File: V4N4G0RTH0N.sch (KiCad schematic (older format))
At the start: 125 parts, among them SW1 SW_Push, U1 ATmega32U4-A, Y1 16MHz

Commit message: I think I'm done??
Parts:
- removed F1, F2: Polyfuse_Small, Fuse:Fuse_1206_3216Metric, symbol V4N4G0RTH0N-rescue:Polyfuse_Small-Device
- removed R3: 10k, Resistor_SMD:R_0805_2012Metric, symbol V4N4G0RTH0N-rescue:R_Small-Device
- removed SW1: SW_Push, random-keyboard-parts:SKQG-1155865, symbol V4N4G0RTH0N-rescue:SW_Push-Switch
- added U2: SRV05-4, Package_TO_SOT_SMD:SOT-23-6, symbol Power_Protection:SRV05-4
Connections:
- wire segments 231 -> 226
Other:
- moved on the sheet: R8, R9

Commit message: V2
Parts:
- added D54: SOD-123, Diode_SMD:D_SOD-123, symbol V4N4G0RTH0N-rescue:D_Small-Device
- added F1: 500mA, symbol Device:Polyfuse_Small
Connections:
- net +5V: now also F1.1
- net GND: now also D54.1 (K)
- net VCC: now also F1.2
- net at U1.13 (~RESET): now also D54.2 (A)
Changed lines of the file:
@@
 Wire Wire Line
 	4600 7450 5000 7450
+$Comp
+L V4N4G0RTH0N-rescue:D_Small-Device D54
+U 1 1 5FDBF20F
+P 1700 2000
+F 0 "D54" H 1600 2150 50  0000 R CNN
+F 1 "SOD-123" H 2000 2150 50  0000 R CNN
+F 2 "Diode_SMD:D_SOD-123" V 1700 2000 50  0001 C CNN
+F 3 "~" V 1700 2000 50  0001 C CNN
+	1    1700 2000
+	1    0    0    -1
+$EndComp
+$Comp
+L V4N4G0RTH0N-rescue:GND-power #PWR01
+U 1 1 5FDE02C4
+P 1350 2000
+F 0 "#PWR01" H 1350 1750 50  0001 C CNN
+F 1 "GND" H 1355 1827 50  0000 C CNN
+F 2 "" H 1350 2000 50  0001 C CNN
+F 3 "" H 1350 2000 50  0001 C CNN
+	1    1350 2000
+	1    0    0    -1
+$EndComp
+Wire Wire Line
+	1350 2000 1600 2000
+Wire Wire Line
+	1800 2000 2000 2000
+$Comp
+L power:VCC #PWR?
+U 1 1 5FF8CE96
+P 1550 9050
+F 0 "#PWR?" H 1550 8900 50  0001 C CNN
+F 1 "VCC" H 1565 9223 50  0000 C CNN
+F 2 "" H 1550 9050 50  0001 C CNN
+F 3 "" H 1550 9050 50  0001 C CNN
+	1    1550 9050
+	1    0    0    -1
+$EndComp
+$Comp
+L power:+5V #PWR?
+U 1 1 5FF8DDFE
+P 2350 9050
+F 0 "#PWR?" H 2350 8900 50  0001 C CNN
+F 1 "+5V" H 2365 9223 50  0000 C CNN
+F 2 "" H 2350 9050 50  0001 C CNN
+F 3 "" H 2350 9050 50  0001 C CNN
+	1    2350 9050
+	1    0    0    -1
+$EndComp
+$Comp
+L Device:Polyfuse_Small F1
+U 1 1 5FF90039
+P 1950 9050
+F 0 "F1" V 1745 9050 50  0000 C CNN
+F 1 "500mA" V 1836 9050 50  0000 C CNN
+F 2 "" H 2000 8850 50  0001 L CNN
+F 3 "~" H 1950 9050 50  0001 C CNN
+	1    1950 9050
+	0    1    1    0
+$EndComp
+Wire Wire Line
+	1550 9050 1850 9050
+Wire Wire Line
+	2050 9050 2350 9050
 $EndSCHEMATC

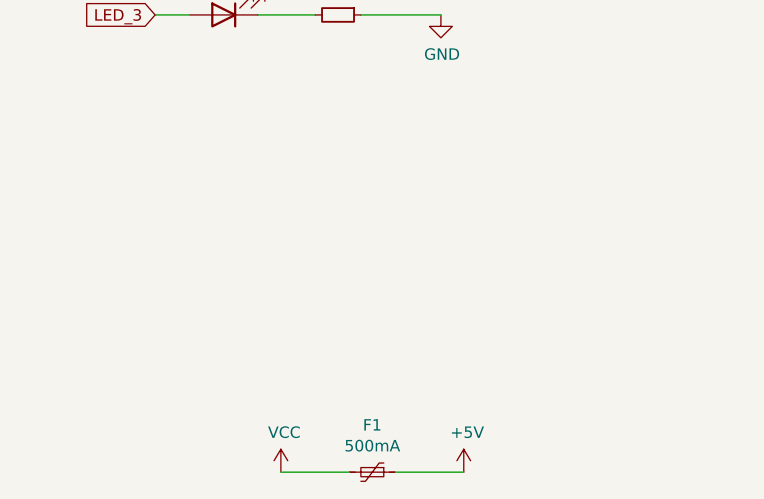
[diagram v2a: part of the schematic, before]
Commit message: V2 sch changes
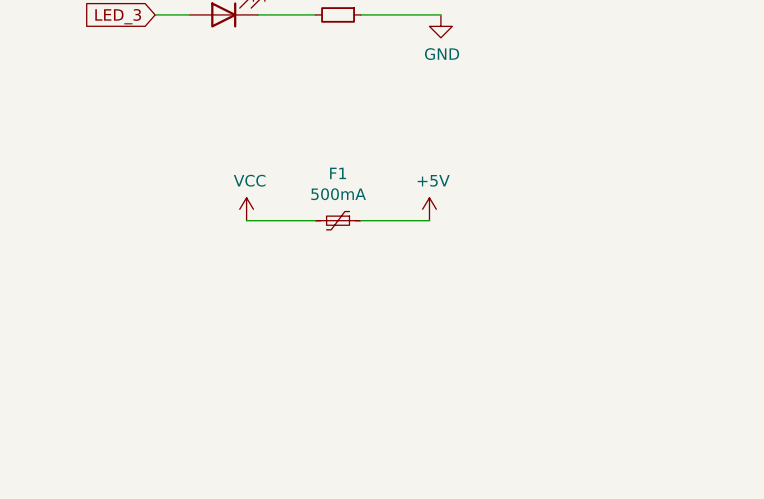
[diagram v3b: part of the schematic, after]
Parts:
- F1: footprint (none) -> Fuse:Fuse_0805_2012Metric
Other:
- moved on the sheet: F1
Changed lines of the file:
@@
 	1800 2000 2000 2000
 $Comp
-L power:VCC #PWR?
+L power:VCC #PWR0109
 U 1 1 5FF8CE96
-P 1550 9050
-F 0 "#PWR?" H 1550 8900 50  0001 C CNN
-F 1 "VCC" H 1565 9223 50  0000 C CNN
-F 2 "" H 1550 9050 50  0001 C CNN
-F 3 "" H 1550 9050 50  0001 C CNN
-	1    1550 9050
+P 1400 7950
+F 0 "#PWR0109" H 1400 7800 50  0001 C CNN
+F 1 "VCC" H 1415 8123 50  0000 C CNN
+F 2 "" H 1400 7950 50  0001 C CNN
+F 3 "" H 1400 7950 50  0001 C CNN
+	1    1400 7950
 	1    0    0    -1
 $EndComp
 $Comp
-L power:+5V #PWR?
+L power:+5V #PWR0110
 U 1 1 5FF8DDFE
-P 2350 9050
-F 0 "#PWR?" H 2350 8900 50  0001 C CNN
-F 1 "+5V" H 2365 9223 50  0000 C CNN
-F 2 "" H 2350 9050 50  0001 C CNN
-F 3 "" H 2350 9050 50  0001 C CNN
-	1    2350 9050
+P 2200 7950
+F 0 "#PWR0110" H 2200 7800 50  0001 C CNN
+F 1 "+5V" H 2215 8123 50  0000 C CNN
+F 2 "" H 2200 7950 50  0001 C CNN
+F 3 "" H 2200 7950 50  0001 C CNN
+	1    2200 7950
 	1    0    0    -1
 $EndComp
@@
 L Device:Polyfuse_Small F1
 U 1 1 5FF90039
-P 1950 9050
-F 0 "F1" V 1745 9050 50  0000 C CNN
-F 1 "500mA" V 1836 9050 50  0000 C CNN
-F 2 "" H 2000 8850 50  0001 L CNN
-F 3 "~" H 1950 9050 50  0001 C CNN
-	1    1950 9050
+P 1800 7950
+F 0 "F1" V 1595 7950 50  0000 C CNN
+F 1 "500mA" V 1686 7950 50  0000 C CNN
+F 2 "Fuse:Fuse_0805_2012Metric" H 1850 7750 50  0001 L CNN
+F 3 "~" H 1800 7950 50  0001 C CNN
+	1    1800 7950
 	0    1    1    0
 $EndComp
 Wire Wire Line
-	1550 9050 1850 9050
+	1400 7950 1700 7950
 Wire Wire Line
-	2050 9050 2350 9050
+	1900 7950 2200 7950
 $EndSCHEMATC

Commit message: V4N v2
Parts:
- added C8: 4.7n, Capacitor_SMD:C_0805_2012Metric, symbol Device:C_Small
- added R10: 1M, Resistor_SMD:R_0805_2012Metric, symbol Device:R_Small
- added R3: 10k, Resistor_SMD:R_0805_2012Metric, symbol Device:R_Small
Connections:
- net +5V: now also R3.1
- net GND: now also C8.1, R10.1; no longer USB1.13 (SHIELD)
- net at D54.2 (A), U1.13 (~RESET): now also R3.2
- new net Earth: C8.2, R10.2, USB1.13 (SHIELD)
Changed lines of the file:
@@
 $EndComp
-Wire Wire Line
-	4500 7450 4600 7450
 Wire Wire Line
 	4500 6750 5650 6750
@@
 Wire Wire Line
 	5700 6300 6200 6300
-Wire Wire Line
-	4500 7550 4600 7550
-Wire Wire Line
-	4600 7550 4600 7450
-Connection ~ 4600 7450
-Wire Wire Line
-	4600 7450 5000 7450
 $Comp
 L V4N4G0RTH0N-rescue:D_Small-Device D54
 U 1 1 5FDBF20F
 P 1700 2000
-F 0 "D54" H 1600 2150 50  0000 R CNN
-F 1 "SOD-123" H 2000 2150 50  0000 R CNN
+F 0 "D54" H 1750 2100 50  0000 R CNN
+F 1 "SOD-123" H 1850 1900 50  0000 R CNN
 F 2 "Diode_SMD:D_SOD-123" V 1700 2000 50  0001 C CNN
 F 3 "~" V 1700 2000 50  0001 C CNN
@@
 	1350 2000 1600 2000
 Wire Wire Line
-	1800 2000 2000 2000
+	1800 2000 1850 2000
 $Comp
 L power:VCC #PWR0109
@@
 Wire Wire Line
 	1900 7950 2200 7950
+$Comp
+L Device:R_Small R3
+U 1 1 5FFE33EE
+P 1850 1700
+F 0 "R3" H 1909 1746 50  0000 L CNN
+F 1 "10k" H 1909 1655 50  0000 L CNN
+F 2 "Resistor_SMD:R_0805_2012Metric" H 1850 1700 50  0001 C CNN
+F 3 "~" H 1850 1700 50  0001 C CNN
+	1    1850 1700
+	1    0    0    -1
+$EndComp
+$Comp
+L power:+5V #PWR0122
+U 1 1 5FFE46B1
+P 1850 1450
+F 0 "#PWR0122" H 1850 1300 50  0001 C CNN
+F 1 "+5V" H 1865 1623 50  0000 C CNN
+F 2 "" H 1850 1450 50  0001 C CNN
+F 3 "" H 1850 1450 50  0001 C CNN
+	1    1850 1450
+	1    0    0    -1
+$EndComp
+Wire Wire Line
+	1850 2000 1850 1800
+Connection ~ 1850 2000
+Wire Wire Line
+	1850 2000 2000 2000
+Wire Wire Line
+	1850 1600 1850 1450
+Wire Wire Line
+	4500 7450 5000 7450
+$Comp
+L power:Earth #PWR0123
+U 1 1 6004768E
+P 4500 7600
+F 0 "#PWR0123" H 4500 7350 50  0001 C CNN
+F 1 "Earth" H 4500 7450 50  0001 C CNN
+F 2 "" H 4500 7600 50  0001 C CNN
+F 3 "~" H 4500 7600 50  0001 C CNN
+	1    4500 7600
+	1    0    0    -1
+$EndComp
+Wire Wire Line
+	4500 7550 4500 7600
+$Comp
+L power:Earth #PWR0124
+U 1 1 60059175
+P 3900 7900
+F 0 "#PWR0124" H 3900 7650 50  0001 C CNN
+F 1 "Earth" H 3900 7750 50  0001 C CNN
+F 2 "" H 3900 7900 50  0001 C CNN
+F 3 "~" H 3900 7900 50  0001 C CNN
+	1    3900 7900
+	0    1    1    0
+$EndComp
+$Comp
+L Device:R_Small R10
+U 1 1 60079CBD
+P 4150 7900
+F 0 "R10" V 3954 7900 50  0000 C CNN
+F 1 "1M" V 4045 7900 50  0000 C CNN
+F 2 "Resistor_SMD:R_0805_2012Metric" H 4150 7900 50  0001 C CNN
+F 3 "~" H 4150 7900 50  0001 C CNN
+	1    4150 7900
+	0    1    1    0
+$EndComp
+$Comp
+L Device:C_Small C8
+U 1 1 6007AEF1
+P 4150 8250
+F 0 "C8" V 3921 8250 50  0000 C CNN
+F 1 "4.7n" V 4012 8250 50  0000 C CNN
+F 2 "Capacitor_SMD:C_0805_2012Metric" H 4150 8250 50  0001 C CNN
+F 3 "~" H 4150 8250 50  0001 C CNN
+	1    4150 8250
+	0    1    1    0
+$EndComp
+$Comp
+L power:GND #PWR0125
+U 1 1 6007C3AC
+P 4400 7900
+F 0 "#PWR0125" H 4400 7650 50  0001 C CNN
+F 1 "GND" V 4405 7772 50  0000 R CNN
+F 2 "" H 4400 7900 50  0001 C CNN
+F 3 "" H 4400 7900 50  0001 C CNN
+	1    4400 7900
+	0    -1   -1   0
+$EndComp
+Wire Wire Line
+	3900 7900 4050 7900
+Wire Wire Line
+	4050 7900 4050 8250
+Connection ~ 4050 7900
+Wire Wire Line
+	4250 8250 4250 7900
+Wire Wire Line
+	4250 7900 4400 7900
+Connection ~ 4250 7900
 $EndSCHEMATC

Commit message: Add slider
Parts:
- added RV1: R_Potentiometer, Potentiometer_THT:Potentiometer_Bourns_PTA3043_Single_Slide, symbol Device:R_Potentiometer
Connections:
- net +5V: now also RV1.3
- net COL11: now also U1.8 (PB0); no longer U1.41 (PF0)
- net GND: now also RV1.1
- new net ANAL_IN: RV1.2, U1.41 (PF0)
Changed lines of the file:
@@
 Text GLabel 3200 4500 2    50   Input ~ 0
 COL10
-Text GLabel 3200 4400 2    50   Input ~ 0
+Text GLabel 3200 2000 2    50   Input ~ 0
 COL11
 Text GLabel 3200 4700 2    50   Input ~ 0
@@
 	4250 7900 4400 7900
 Connection ~ 4250 7900
+$Comp
+L Device:R_Potentiometer RV1
+U 1 1 6051941E
+P 1300 5500
+F 0 "RV1" V 1093 5500 50  0000 C CNN
+F 1 "R_Potentiometer" V 1184 5500 50  0000 C CNN
+F 2 "Potentiometer_THT:Potentiometer_Bourns_PTA3043_Single_Slide" H 1300 5500 50  0001 C CNN
+F 3 "~" H 1300 5500 50  0001 C CNN
+	1    1300 5500
+	0    1    1    0
+$EndComp
+$Comp
+L power:GND #PWR0126
+U 1 1 6051C5EA
+P 1600 5550
+F 0 "#PWR0126" H 1600 5300 50  0001 C CNN
+F 1 "GND" H 1605 5377 50  0000 C CNN
+F 2 "" H 1600 5550 50  0001 C CNN
+F 3 "" H 1600 5550 50  0001 C CNN
+	1    1600 5550
+	1    0    0    -1
+$EndComp
+Wire Wire Line
+	1450 5500 1600 5500
+Wire Wire Line
+	1600 5500 1600 5550
+$Comp
+L power:+5V #PWR0127
+U 1 1 6053121A
+P 900 5500
+F 0 "#PWR0127" H 900 5350 50  0001 C CNN
+F 1 "+5V" H 915 5673 50  0000 C CNN
+F 2 "" H 900 5500 50  0001 C CNN
+F 3 "" H 900 5500 50  0001 C CNN
+	1    900  5500
+	1    0    0    -1
+$EndComp
+Wire Wire Line
+	1150 5500 900  5500
+Text GLabel 1200 5750 0    50   Input ~ 0
+ANAL_IN
+Wire Wire Line
+	1200 5750 1300 5750
+Wire Wire Line
+	1300 5750 1300 5650
+Text GLabel 3200 4400 2    50   Input ~ 0
+ANAL_IN
 $EndSCHEMATC
